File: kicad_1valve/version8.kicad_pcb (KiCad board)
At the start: 2 copper layers, 49.5 x 33 mm, 19 parts, among them J1 valve out, J2 12V in, J3 sense, U1 stepdown, U2 WeMos_mini, U3 DS18B20

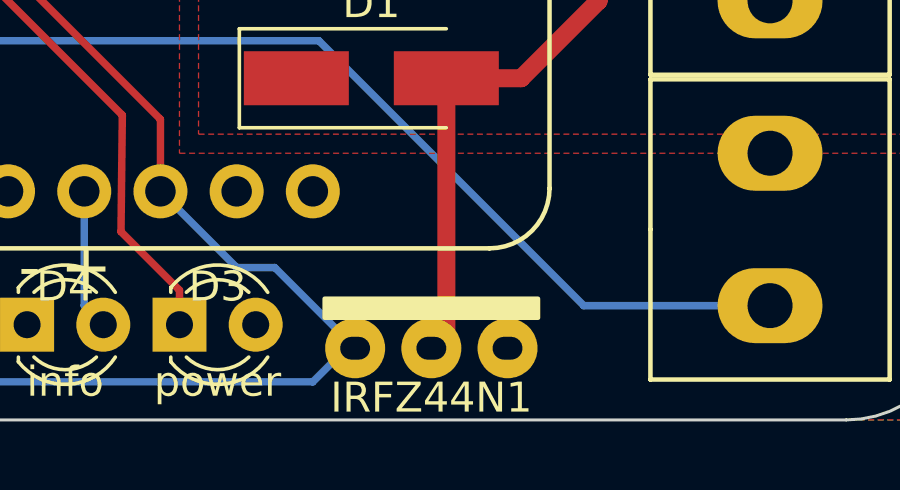
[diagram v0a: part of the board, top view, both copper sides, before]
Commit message: use propper symbol and footprint for irlz44n
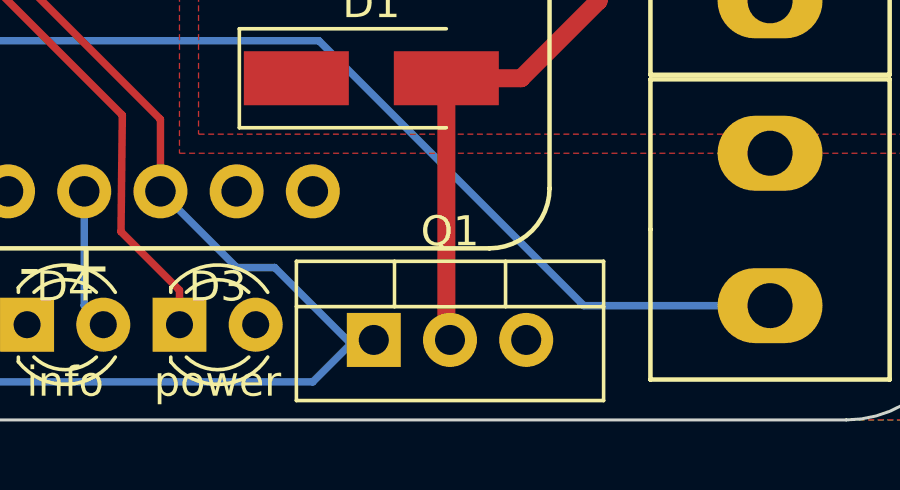
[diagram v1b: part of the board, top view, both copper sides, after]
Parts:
- removed IRFZ44N1: , custom:irlz44n_vertical
- added Q1: IRLZ44N, TO_SOT_Packages_THT:TO-220-3_Vertical, F.Cu at (148.1, 69.7)
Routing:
- net Net-(D1-Pad2): track 27.9 -> 27.2 mm
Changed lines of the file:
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@@
     (thickness 1.6)
     (drawings 17)
-    (tracks 66)
+    (tracks 65)
     (zones 0)
     (modules 19)
@@
     )
   )
-  (module custom:irlz44n_vertical (layer F.Cu)
-    (at 150 70 270)
-    (fp_text reference IRFZ44N1 (at 1.651 0 180) (layer F.SilkS)
-      (effects (font (size 1 1) (thickness 0.15)))
-    )
-    (fp_text value " " (at 0 -0.5 270) (layer F.Fab)
-      (effects (font (size 1 1) (thickness 0.15)))
-    )
-    (fp_poly (pts (xy -1.651 -3.556) (xy -1.651 3.556) (xy -1.016 3.556) (xy -1.016 -3.556)) (layer F.SilkS) (width 0.15))
-    (pad 2 thru_hole circle (at 0 2.54 270) (size 2 2) (drill oval 0.762 1) (layers *.Cu *.Mask)
-      (net 18 valve))
-    (pad 3 thru_hole circle (at 0 0 270) (size 2 2) (drill oval 0.762 1) (layers *.Cu *.Mask)
-      (net 1 "Net-(D1-Pad2)"))
-    (pad 1 thru_hole circle (at 0 -2.54 270) (size 2 2) (drill oval 0.762 1) (layers *.Cu *.Mask)
-      (net 7 GND))
-  )
   (module custom:termina_2pin (layer F.Cu)
     (at 161.29 45.72 90)
@@
       (net 7 GND))
   )
+  (module TO_SOT_Packages_THT:TO-220-3_Vertical (layer F.Cu)
+    (at 148.082 69.723)
+    (descr "TO-220-3, Vertical, RM 2.54mm")
+    (tags "TO-220-3 Vertical RM 2.54mm")
+    (fp_text reference Q1 (at 2.54 -3.62) (layer F.SilkS)
+      (effects (font (size 1 1) (thickness 0.15)))
+    )
+    (fp_text value IRLZ44N (at 2.54 3.92) (layer F.Fab)
+      (effects (font (size 1 1) (thickness 0.15)))
+    )
+    (fp_line (start 7.79 -2.75) (end -2.71 -2.75) (layer F.CrtYd) (width 0.05))
+    (fp_line (start 7.79 2.16) (end 7.79 -2.75) (layer F.CrtYd) (width 0.05))
+    (fp_line (start -2.71 2.16) (end 7.79 2.16) (layer F.CrtYd) (width 0.05))
+    (fp_line (start -2.71 -2.75) (end -2.71 2.16) (layer F.CrtYd) (width 0.05))
+    (fp_line (start 4.391 -2.62) (end 4.391 -1.11) (layer F.SilkS) (width 0.12))
+    (fp_line (start 0.69 -2.62) (end 0.69 -1.11) (layer F.SilkS) (width 0.12))
+    (fp_line (start -2.58 -1.11) (end 7.66 -1.11) (layer F.SilkS) (width 0.12))
+    (fp_line (start 7.66 -2.62) (end 7.66 2.021) (layer F.SilkS) (width 0.12))
+    (fp_line (start -2.58 -2.62) (end -2.58 2.021) (layer F.SilkS) (width 0.12))
+    (fp_line (start -2.58 2.021) (end 7.66 2.021) (layer F.SilkS) (width 0.12))
+    (fp_line (start -2.58 -2.62) (end 7.66 -2.62) (layer F.SilkS) (width 0.12))
+    (fp_line (start 4.39 -2.5) (end 4.39 -1.23) (layer F.Fab) (width 0.1))
+    (fp_line (start 0.69 -2.5) (end 0.69 -1.23) (layer F.Fab) (width 0.1))
+    (fp_line (start -2.46 -1.23) (end 7.54 -1.23) (layer F.Fab) (width 0.1))
+    (fp_line (start 7.54 -2.5) (end -2.46 -2.5) (layer F.Fab) (width 0.1))
+    (fp_line (start 7.54 1.9) (end 7.54 -2.5) (layer F.Fab) (width 0.1))
+    (fp_line (start -2.46 1.9) (end 7.54 1.9) (layer F.Fab) (width 0.1))
+    (fp_line (start -2.46 -2.5) (end -2.46 1.9) (layer F.Fab) (width 0.1))
+    (fp_text user %R (at 2.54 -3.62) (layer F.Fab)
+      (effects (font (size 1 1) (thickness 0.15)))
+    )
+    (pad 3 thru_hole oval (at 5.08 0) (size 1.8 1.8) (drill 1) (layers *.Cu *.Mask)
+      (net 7 GND))
+    (pad 2 thru_hole oval (at 2.54 0) (size 1.8 1.8) (drill 1) (layers *.Cu *.Mask)
+      (net 1 "Net-(D1-Pad2)"))
+    (pad 1 thru_hole rect (at 0 0) (size 1.8 1.8) (drill 1) (layers *.Cu *.Mask)
+      (net 18 valve))
+    (model ${KISYS3DMOD}/TO_SOT_Packages_THT.3dshapes/TO-220-3_Vertical.wrl
+      (offset (xyz 2.539999961853027 0 0))
+      (scale (xyz 0.393701 0.393701 0.393701))
+      (rotate (xyz 0 0 0))
+    )
+  )
   (gr_text version (at 121.666 41.0845 90) (layer F.SilkS)
     (effects (font (size 0.3 0.3) (thickness 0.05)))
@@
   (segment (start 152.995 61) (end 150.5 61) (width 0.6) (layer F.Cu) (net 1))
   (segment (start 155.575 53.975) (end 155.575 58.42) (width 0.6) (layer F.Cu) (net 1))
-  (segment (start 150.5 69.5) (end 150 70) (width 0.6) (layer F.Cu) (net 1))
   (segment (start 150.5 61) (end 150.5 69.5) (width 0.6) (layer F.Cu) (net 1))
-  (segment (start 140.97 64.77) (end 143.51 67.31) (width 0.25) (layer B.Cu) (net 18))
-  (segment (start 144.78 67.31) (end 147.32 69.85) (width 0.25) (layer B.Cu) (net 18))
-  (segment (start 143.51 67.31) (end 144.78 67.31) (width 0.25) (layer B.Cu) (net 18))
-  (segment (start 133.985 69.215) (end 133.985 70.485) (width 0.25) (layer B.Cu) (net 18))
-  (segment (start 133.985 70.485) (end 134.62 71.12) (width 0.25) (layer B.Cu) (net 18))
-  (segment (start 134.62 71.12) (end 146.05 71.12) (width 0.25) (layer B.Cu) (net 18))
-  (segment (start 146.05 71.12) (end 147.32 69.85) (width 0.25) (layer B.Cu) (net 18))
-  (segment (start 140.97 62.370002) (end 140.97 64.77) (width 0.25) (layer F.Cu) (net 18))
-  (segment (start 124.29 44.45) (end 124.29 45.690002) (width 0.25) (layer F.Cu) (net 18))
-  (segment (start 124.29 45.690002) (end 140.97 62.370002) (width 0.25) (layer F.Cu) (net 18))
   (segment (start 130.295 69.215) (end 125.73 64.65) (width 0.25) (layer B.Cu) (net 3))
   (segment (start 131.445 69.215) (end 130.295 69.215) (width 0.25) (layer B.Cu) (net 3))
@@
   (segment (start 126.365 62.865) (end 125.095 61.595) (width 0.25) (layer F.Cu) (net 6))
   (segment (start 127.635 66.675) (end 126.365 65.405) (width 0.25) (layer F.Cu) (net 6))
-  (segment (start 138.43 68.58) (end 139.065 69.215) (width 0.25) (layer B.Cu) (net 19))
-  (segment (start 138.43 64.77) (end 138.43 68.58) (width 0.25) (layer B.Cu) (net 19))
   (segment (start 122.09 44.45) (end 122.09 50.165) (width 0.25) (layer F.Cu) (net 7))
   (segment (start 122.09 50.165) (end 122.09 55.88) (width 0.25) (layer F.Cu) (net 7))
   (via (at 122.09 50.165) (size 0.8) (drill 0.4) (layers F.Cu B.Cu) (net 7))
+  (segment (start 142.24 43.18) (end 140.97 41.91) (width 0.25) (layer F.Cu) (net 8))
+  (segment (start 151.13 43.18) (end 142.24 43.18) (width 0.25) (layer F.Cu) (net 8))
+  (segment (start 146.4056 41.5544) (end 146.05 41.91) (width 0.25) (layer F.Cu) (net 9))
+  (segment (start 151.13 41.5544) (end 146.4056 41.5544) (width 0.25) (layer F.Cu) (net 9))
+  (segment (start 140.97 64.77) (end 143.51 67.31) (width 0.25) (layer B.Cu) (net 18))
+  (segment (start 144.78 67.31) (end 147.32 69.85) (width 0.25) (layer B.Cu) (net 18))
+  (segment (start 143.51 67.31) (end 144.78 67.31) (width 0.25) (layer B.Cu) (net 18))
+  (segment (start 133.985 69.215) (end 133.985 70.485) (width 0.25) (layer B.Cu) (net 18))
+  (segment (start 133.985 70.485) (end 134.62 71.12) (width 0.25) (layer B.Cu) (net 18))
+  (segment (start 134.62 71.12) (end 146.05 71.12) (width 0.25) (layer B.Cu) (net 18))
+  (segment (start 146.05 71.12) (end 147.32 69.85) (width 0.25) (layer B.Cu) (net 18))
+  (segment (start 140.97 62.370002) (end 140.97 64.77) (width 0.25) (layer F.Cu) (net 18))
+  (segment (start 124.29 44.45) (end 124.29 45.690002) (width 0.25) (layer F.Cu) (net 18))
+  (segment (start 124.29 45.690002) (end 140.97 62.370002) (width 0.25) (layer F.Cu) (net 18))
+  (segment (start 138.43 68.58) (end 139.065 69.215) (width 0.25) (layer B.Cu) (net 19))
+  (segment (start 138.43 64.77) (end 138.43 68.58) (width 0.25) (layer B.Cu) (net 19))
   (via (at 129.5 59.75) (size 0.8) (drill 0.4) (layers F.Cu B.Cu) (net 20))
   (segment (start 124.29 59.69) (end 129.44 59.69) (width 0.25) (layer F.Cu) (net 20))
@@
   (segment (start 135.89 53.36) (end 135.89 41.91) (width 0.25) (layer B.Cu) (net 20))
   (segment (start 129.5 59.75) (end 135.89 53.36) (width 0.25) (layer B.Cu) (net 20))
-  (segment (start 142.24 43.18) (end 140.97 41.91) (width 0.25) (layer F.Cu) (net 8))
-  (segment (start 151.13 43.18) (end 142.24 43.18) (width 0.25) (layer F.Cu) (net 8))
-  (segment (start 146.4056 41.5544) (end 146.05 41.91) (width 0.25) (layer F.Cu) (net 9))
-  (segment (start 151.13 41.5544) (end 146.4056 41.5544) (width 0.25) (layer F.Cu) (net 9))
   (segment (start 125.095 67.800787) (end 125.095 69.215) (width 0.25) (layer F.Cu) (net 21))
   (segment (start 125.095 66.355) (end 125.095 67.800787) (width 0.25) (layer F.Cu) (net 21))
